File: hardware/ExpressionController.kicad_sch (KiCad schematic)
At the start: 0 parts

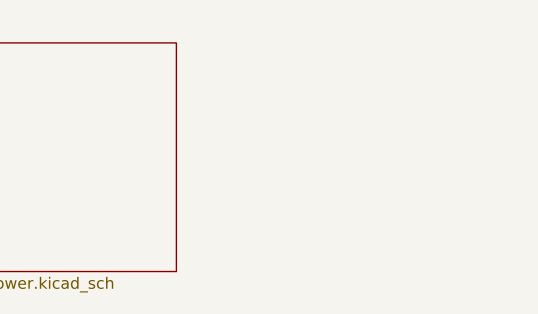
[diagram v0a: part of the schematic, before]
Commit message: reworked power protection circuit and fixed ERC errors
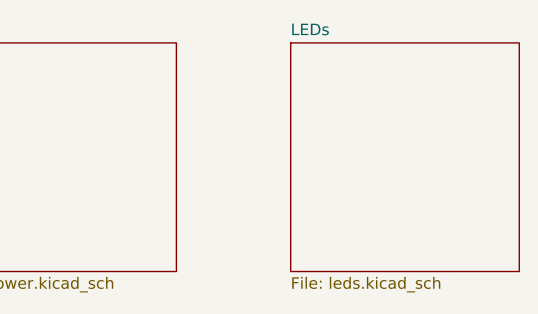
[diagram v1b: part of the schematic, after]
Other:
- added sheet LEDs (leds.kicad_sch)
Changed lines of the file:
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@@
 	(paper "A4")
+	(sheet
+		(at 139.7 25.4)
+		(size 25.4 25.4)
+		(exclude_from_sim no)
+		(in_bom yes)
+		(on_board yes)
+		(dnp no)
+		(fields_autoplaced yes)
+		(stroke
+			(width 0.1524)
+			(type solid)
+		)
+		(fill
+			(color 0 0 0 0)
+		)
+		(property "Sheetname" "LEDs"
+			(at 139.7 24.6884 0)
+			(show_name no)
+			(do_not_autoplace no)
+			(effects
+				(font
+					(size 1.27 1.27)
+				)
+				(justify left bottom)
+			)
+		)
+		(property "Sheetfile" "leds.kicad_sch"
+			(at 139.7 51.3846 0)
+			(show_name no)
+			(do_not_autoplace no)
+			(effects
+				(font
+					(size 1.27 1.27)
+				)
+				(justify left top)
+			)
+		)
+		(instances
+			(project "ExpressionController"
+				(path "/acb9d00b-1122-4203-9813-1d558ab77d86"
+					(page "9")
+				)
+			)
+		)
+	)
 	(sheet
 		(at 25.4 25.4)

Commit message: added signed declaration and updated schematic names
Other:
- company: (none) -> Amon Benson, TU Berlin
- title: (none) -> Expression Adapter
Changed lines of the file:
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@@
 	(generator_version "10.0")
 	(paper "A4")
+	(title_block
+		(title "Expression Adapter")
+		(date "2026-09-27")
+		(rev "1.0")
+		(company "Amon Benson, TU Berlin")
+	)
 	(sheet
 		(at 139.7 25.4)
